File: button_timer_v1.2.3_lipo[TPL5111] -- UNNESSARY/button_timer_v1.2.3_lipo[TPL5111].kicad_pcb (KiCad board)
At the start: 2 copper layers, 21 x 41.7 mm, 24 parts, among them J1 Conn_01x05_Female, Q1 mmbt2222, SW1 SW_Push, SW2 SW_Push, U2 AP2112K-3.3, U3 TPL5111, X1 ESP-12E

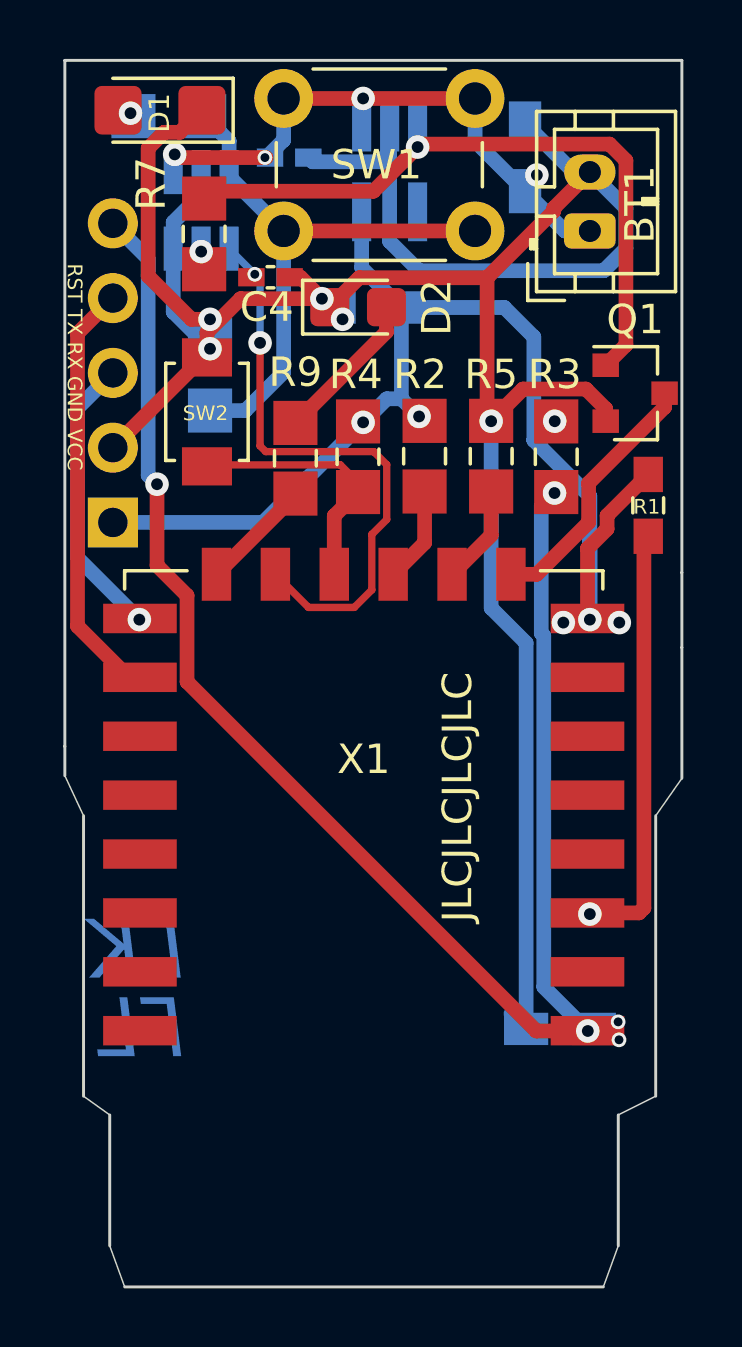
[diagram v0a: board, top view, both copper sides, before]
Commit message: cap between esp vcc and ground added
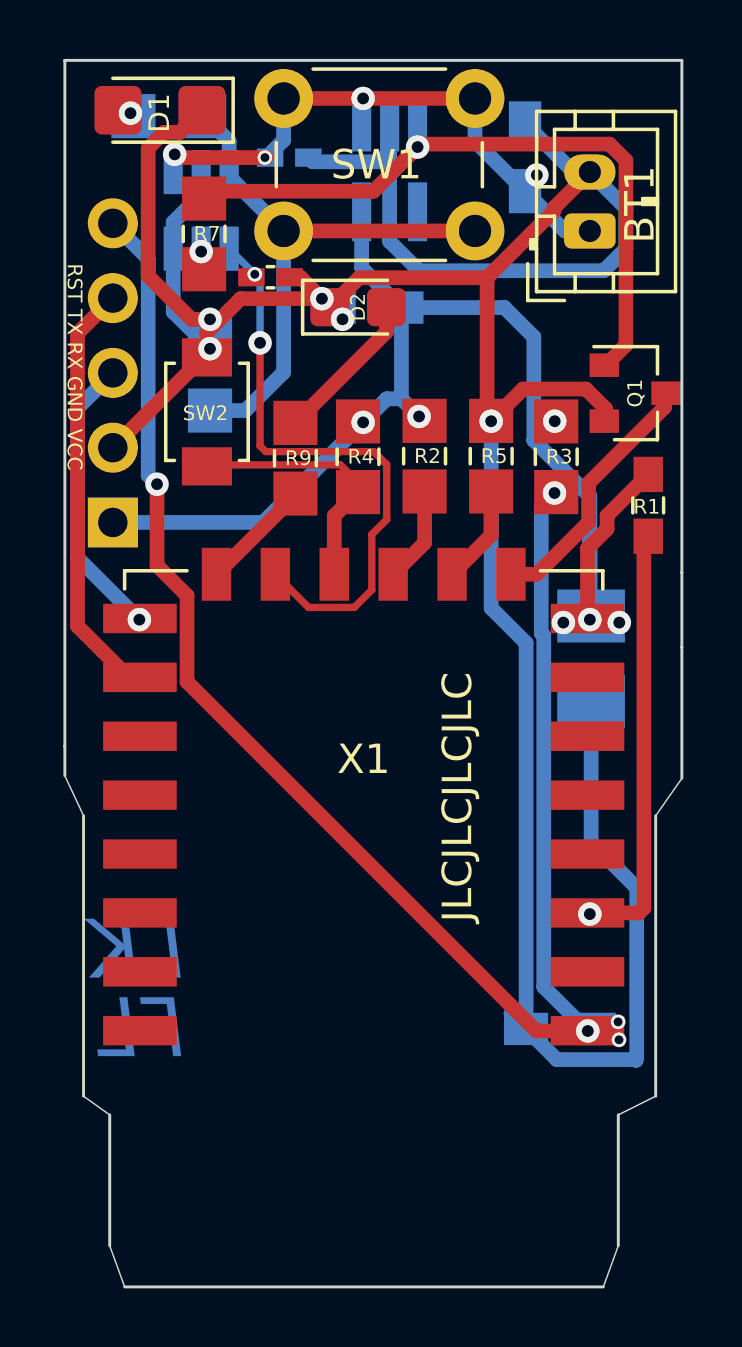
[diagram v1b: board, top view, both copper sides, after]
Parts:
- added C6: TAJB476M010TNJ, SamacSys_Parts:CAPPM3528X210N, B.Cu at (133.4, 81.0)
- D2: footprint LED_SMD:LED_0805_2012Metric_Castellated -> handsolder:LED_0805_2012Metric_Castellated_mod
- Q1: footprint Package_TO_SOT_SMD:SOT-23 -> handsolder:SOT-23
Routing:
- net /GND: track 92.8 -> 109.8 mm
